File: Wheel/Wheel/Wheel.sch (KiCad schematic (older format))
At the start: 124 parts, among them J1 Conn_02x09_Odd_Even, J10 RJ45, J11 Screw_Terminal_01x02, J12 DS-201, J13 Conn_01x04, J14 Conn_02x13_Top_Bottom, J15 DB25_Female, J16 Conn_01x06, J17 Conn_01x07, J18 Conn_01x06, J19 RJ45, J2 RJ45, J20 DB9_Male, J21 DB9_Female, J3 RJ45, J4 RJ45, J5 USB_B, J6 Conn_02x10_Odd_Even, J7 Conn_02x09_Odd_Even, J8 RJ45, J9 RJ45, U1 MCP23S17_SP, U10 PC817, U11 IP4220CZ6, U12 PC817, U13 IP4220CZ6, U2 STM32F407VETx, U3 MCP23S17_SP, U4 USBLC6-2SC6, U5 AMS1117, U6 4N35, U7 PC817, U8 PC817, U9 PC817, Y1 32,768 кГц, Y2 8MHz

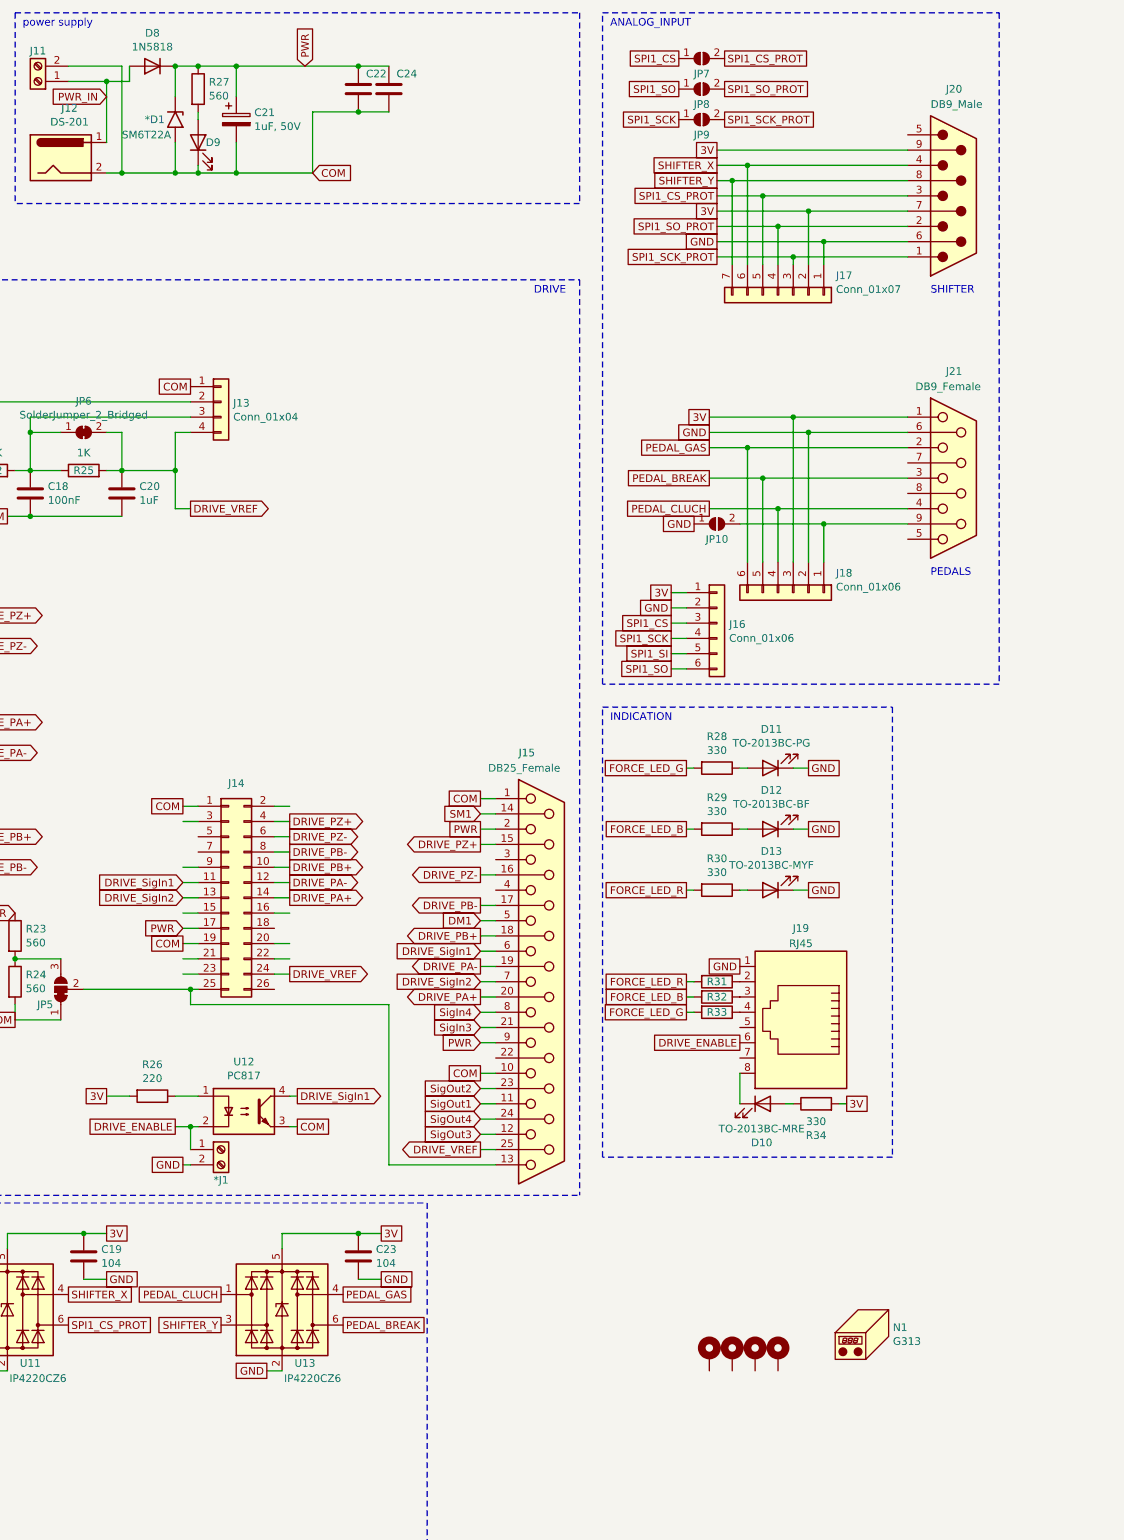
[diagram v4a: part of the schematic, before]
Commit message: I've added a connector for connect STM32F407G-DISK1 to the Wheel board
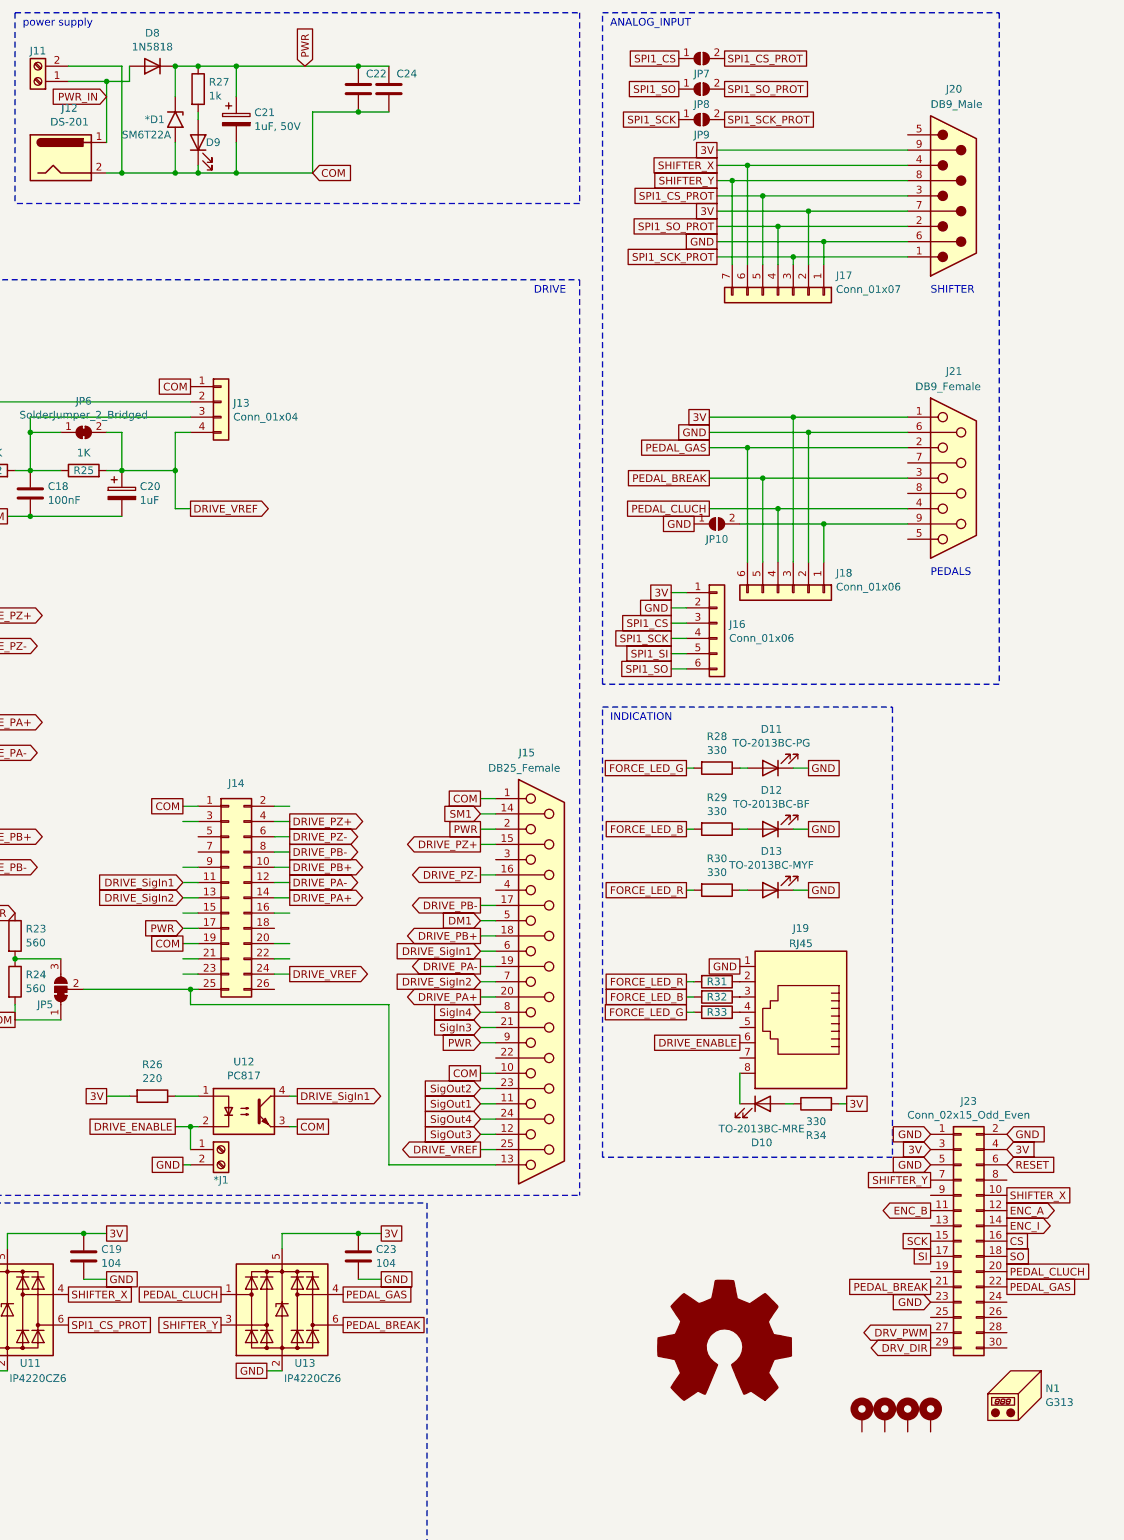
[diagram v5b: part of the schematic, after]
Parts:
- removed C20: 1uF, Capacitor_SMD:C_0805_2012Metric, symbol Device:C
- added C20: 1uF, Capacitor_THT:CP_Radial_D5.0mm_P2.00mm, symbol Device:CP
- added J23: Conn_02x15_Odd_Even, Connector_PinHeader_2.54mm:PinHeader_2x15_P2.54mm_Vertical, symbol Connector_Generic:Conn_02x15_Odd_Even
- added LOGO1: Logo_Open_Hardware_Large, Symbol:OSHW-Logo2_14.6x12mm_SilkScreen, symbol Graphic:Logo_Open_Hardware_Large
- R27: value 560 -> 1k
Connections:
- net 3V: now also J23.3 (Pin_3), J23.4 (Pin_4)
- net COM: now also C20.2
- net CS: now also J23.16 (Pin_16)
- net DRIVE_VREF: now also C20.1
- net DRV_DIR: now also J23.29 (Pin_29)
- net DRV_PWM: now also J23.27 (Pin_27)
- net ENC_A: now also J23.12 (Pin_12)
- net ENC_B: now also J23.11 (Pin_11)
- net ENC_I: now also J23.14 (Pin_14)
- net GND: now also J23.1 (Pin_1), J23.2 (Pin_2), J23.23 (Pin_23), J23.5 (Pin_5)
- net PEDAL_BREAK: now also J23.21 (Pin_21)
- net PEDAL_CLUCH: now also J23.20 (Pin_20)
- net PEDAL_GAS: now also J23.22 (Pin_22)
- net RESET: now also J23.6 (Pin_6)
- net SCK: now also J23.15 (Pin_15)
- net SHIFTER_X: now also J23.10 (Pin_10)
- net SHIFTER_Y: now also J23.7 (Pin_7)
- net SI: now also J23.17 (Pin_17)
- net SO: now also J23.18 (Pin_18)
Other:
- moved on the sheet: N1
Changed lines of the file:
@@
 P 10200 1050
 F 0 "R27" H 10270 1096 50  0000 L CNN
-F 1 "560" H 10270 1005 50  0000 L CNN
+F 1 "1k" H 10270 1005 50  0000 L CNN
 F 2 "Resistor_SMD:R_0805_2012Metric" V 10130 1050 50  0001 C CNN
 F 3 "https://www.chipdip.ru/product0/9000079474" H 10200 1050 50  0001 C CNN
@@
 L Mechanical:MountingHole_Pad H4
 U 1 1 60EF3A16
-P 14000 9350
-F 0 "H4" H 14100 9399 50  0001 L CNN
-F 1 "MountingHole_Pad" H 14100 9308 50  0001 L CNN
-F 2 "MountingHole:MountingHole_3.2mm_M3_Pad" H 14000 9350 50  0001 C CNN
-F 3 "~" H 14000 9350 50  0001 C CNN
-	1    14000 9350
+P 15000 9750
+F 0 "H4" H 15100 9799 50  0001 L CNN
+F 1 "MountingHole_Pad" H 15100 9708 50  0001 L CNN
+F 2 "MountingHole:MountingHole_3.2mm_M3_Pad" H 15000 9750 50  0001 C CNN
+F 3 "~" H 15000 9750 50  0001 C CNN
+	1    15000 9750
 	1    0    0    -1
 $EndComp
@@
 L Mechanical:MountingHole_Pad H3
 U 1 1 60EF7343
-P 13850 9350
-F 0 "H3" H 13950 9399 50  0001 L CNN
-F 1 "MountingHole_Pad" H 13950 9308 50  0001 L CNN
-F 2 "MountingHole:MountingHole_3.2mm_M3_Pad" H 13850 9350 50  0001 C CNN
-F 3 "~" H 13850 9350 50  0001 C CNN
-	1    13850 9350
+P 14850 9750
+F 0 "H3" H 14950 9799 50  0001 L CNN
+F 1 "MountingHole_Pad" H 14950 9708 50  0001 L CNN
+F 2 "MountingHole:MountingHole_3.2mm_M3_Pad" H 14850 9750 50  0001 C CNN
+F 3 "~" H 14850 9750 50  0001 C CNN
+	1    14850 9750
 	1    0    0    -1
 $EndComp
@@
 L Mechanical:MountingHole_Pad H2
 U 1 1 60EF760B
-P 13700 9350
-F 0 "H2" H 13800 9399 50  0001 L CNN
-F 1 "MountingHole_Pad" H 13800 9308 50  0001 L CNN
-F 2 "MountingHole:MountingHole_3.2mm_M3_Pad" H 13700 9350 50  0001 C CNN
-F 3 "~" H 13700 9350 50  0001 C CNN
-	1    13700 9350
+P 14700 9750
+F 0 "H2" H 14800 9799 50  0001 L CNN
+F 1 "MountingHole_Pad" H 14800 9708 50  0001 L CNN
+F 2 "MountingHole:MountingHole_3.2mm_M3_Pad" H 14700 9750 50  0001 C CNN
+F 3 "~" H 14700 9750 50  0001 C CNN
+	1    14700 9750
 	1    0    0    -1
 $EndComp
@@
 L Mechanical:MountingHole_Pad H1
 U 1 1 60EF780C
-P 13550 9350
-F 0 "H1" H 13650 9399 50  0001 L CNN
-F 1 "MountingHole_Pad" H 13650 9308 50  0001 L CNN
-F 2 "MountingHole:MountingHole_3.2mm_M3_Pad" H 13550 9350 50  0001 C CNN
-F 3 "~" H 13550 9350 50  0001 C CNN
-	1    13550 9350
+P 14550 9750
+F 0 "H1" H 14650 9799 50  0001 L CNN
+F 1 "MountingHole_Pad" H 14650 9708 50  0001 L CNN
+F 2 "MountingHole:MountingHole_3.2mm_M3_Pad" H 14550 9750 50  0001 C CNN
+F 3 "~" H 14550 9750 50  0001 C CNN
+	1    14550 9750
 	1    0    0    -1
 $EndComp
@@
 	1    9450 3550
 	0    -1   -1   0
-$EndComp
-$Comp
-L Device:C C20
-U 1 1 600085E0
-P 9700 3700
-F 0 "C20" H 9815 3746 50  0000 L CNN
-F 1 "1uF" H 9815 3655 50  0000 L CNN
-F 2 "Capacitor_SMD:C_0805_2012Metric" H 9738 3550 50  0001 C CNN
-F 3 "https://www.chipdip.ru/product/grm21br71c105k" H 9700 3700 50  0001 C CNN
-	1    9700 3700
-	1    0    0    -1
 $EndComp
 Wire Wire Line
@@
 L Mechanical:Housing N1
 U 1 1 60618C70
-P 14600 9200
-F 0 "N1" H 14753 9234 50  0000 L CNN
-F 1 "G313" H 14753 9143 50  0000 L CNN
-F 2 "cases:CASE_G313" H 14650 9250 50  0001 C CNN
-F 3 "~" H 14650 9250 50  0001 C CNN
-	1    14600 9200
+P 15600 9600
+F 0 "N1" H 15753 9634 50  0000 L CNN
+F 1 "G313" H 15753 9543 50  0000 L CNN
+F 2 "cases:CASE_G313" H 15650 9650 50  0001 C CNN
+F 3 "~" H 15650 9650 50  0001 C CNN
+	1    15600 9600
 	1    0    0    -1
 $EndComp
@@
 Wire Wire Line
 	13600 1750 13900 1750
+Connection ~ 13900 1750
+Text GLabel 13650 850  2    50   UnSpc ~ 0
+SPI1_CS_PROT
+Text GLabel 13650 1050 2    50   UnSpc ~ 0
+SPI1_SO_PROT
+Text GLabel 13650 1250 2    50   UnSpc ~ 0
+SPI1_SCK_PROT
+$Comp
+L Connector_Generic:Conn_02x15_Odd_Even J23
+U 1 1 603B8041
+P 15200 8600
+F 0 "J23" H 15250 9517 50  0000 C CNN
+F 1 "Conn_02x15_Odd_Even" H 15250 9426 50  0000 C CNN
+F 2 "Connector_PinHeader_2.54mm:PinHeader_2x15_P2.54mm_Vertical" H 15200 8600 50  0001 C CNN
+F 3 "~" H 15200 8600 50  0001 C CNN
+	1    15200 8600
+	1    0    0    -1
+$EndComp
+Text GLabel 15000 7900 0    50   Input ~ 0
+GND
+Text GLabel 15500 7900 2    50   Input ~ 0
+GND
+Text GLabel 15000 8000 0    50   Input ~ 0
+3V
+Text GLabel 15500 8000 2    50   Input ~ 0
+3V
+Text GLabel 15000 8100 0    50   Input ~ 0
+GND
+Text GLabel 15000 8200 0    50   UnSpc ~ 0
+SHIFTER_Y
+Text GLabel 15000 8400 0    50   Output ~ 0
+ENC_B
+Text GLabel 15000 8600 0    50   UnSpc ~ 0
+SCK
+Text GLabel 15000 8700 0    50   UnSpc ~ 0
+SI
+Text GLabel 15000 8900 0    50   UnSpc ~ 0
+PEDAL_BREAK
+Text GLabel 15000 9000 0    50   Input ~ 0
+GND
+Text GLabel 15000 9200 0    50   Output ~ 0
+DRV_PWM
+Text GLabel 15000 9300 0    50   Output ~ 0
+DRV_DIR
+Text GLabel 15500 8100 2    50   Input ~ 0
+RESET
+Text GLabel 15500 8300 2    50   UnSpc ~ 0
+SHIFTER_X
+Text GLabel 15500 8400 2    50   Output ~ 0
+ENC_A
+Text GLabel 15500 8500 2    50   Output ~ 0
+ENC_I
+Text GLabel 15500 8600 2    50   UnSpc ~ 0
+CS
+Text GLabel 15500 8700 2    50   UnSpc ~ 0
+SO
+Text GLabel 15500 8800 2    50   UnSpc ~ 0
+PEDAL_CLUCH
+Text GLabel 15500 8900 2    50   UnSpc ~ 0
+PEDAL_GAS
+$Comp
+L Graphic:Logo_Open_Hardware_Large LOGO1
+U 1 1 6057E655
+P 13650 9300
+F 0 "LOGO1" H 13650 9800 50  0001 C CNN
+F 1 "Logo_Open_Hardware_Large" H 13650 8900 50  0001 C CNN
+F 2 "Symbol:OSHW-Logo2_14.6x12mm_SilkScreen" H 13650 9300 50  0001 C CNN
+F 3 "~" H 13650 9300 50  0001 C CNN
+	1    13650 9300
+	1    0    0    -1
+$EndComp
+$Comp
+L Device:CP C20
+U 1 1 600C4636
+P 9700 3700
+F 0 "C20" H 9818 3746 50  0000 L CNN
+F 1 "1uF" H 9818 3655 50  0000 L CNN
+F 2 "Capacitor_THT:CP_Radial_D5.0mm_P2.00mm" H 9738 3550 50  0001 C CNN
+F 3 "https://www.chipdip.ru/product0/9000565812" H 9700 3700 50  0001 C CNN
+F 4 "JRB2A010M02000500110000B" H 9700 3700 50  0001 C CNN "PN"
+	1    9700 3700
+	1    0    0    -1
+$EndComp
 Wire Bus Line
 	4450 9500 4450 10400
@@
 Wire Bus Line
 	2650 7500 2650 10500
-Connection ~ 13900 1750
-Text GLabel 13650 850  2    50   UnSpc ~ 0
-SPI1_CS_PROT
-Text GLabel 13650 1050 2    50   UnSpc ~ 0
-SPI1_SO_PROT
-Text GLabel 13650 1250 2    50   UnSpc ~ 0
-SPI1_SCK_PROT
 $EndSCHEMATC
